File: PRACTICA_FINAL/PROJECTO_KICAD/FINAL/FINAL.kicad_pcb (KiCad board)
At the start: 4 copper layers, 100 x 56 mm, 111 parts, among them IC1 FT2232H, SW1 SWITCH-2CH-6P-3010010P1, SW2 EVQQ2, U1 ARDUINO_MEGA_SHIELD, U101 ATMEGA32U4-XUMU, U2 LTC3419MS, U3 93C56B, X1 12MHz, Y1 16Mhz KX-7

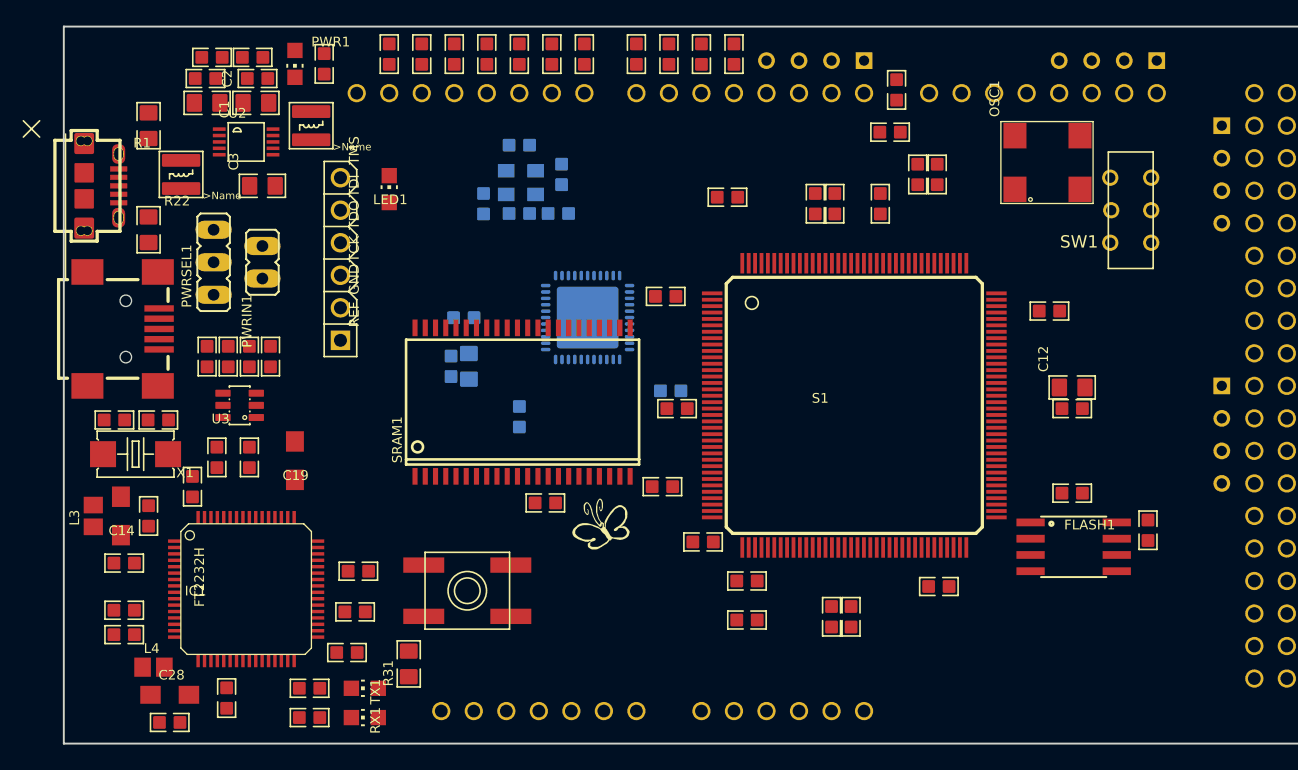
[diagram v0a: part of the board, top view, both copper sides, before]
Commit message: Agregados ultimos modelos 3D y tambien los agujeros de sujecion hasta aca estaria el trabajo.
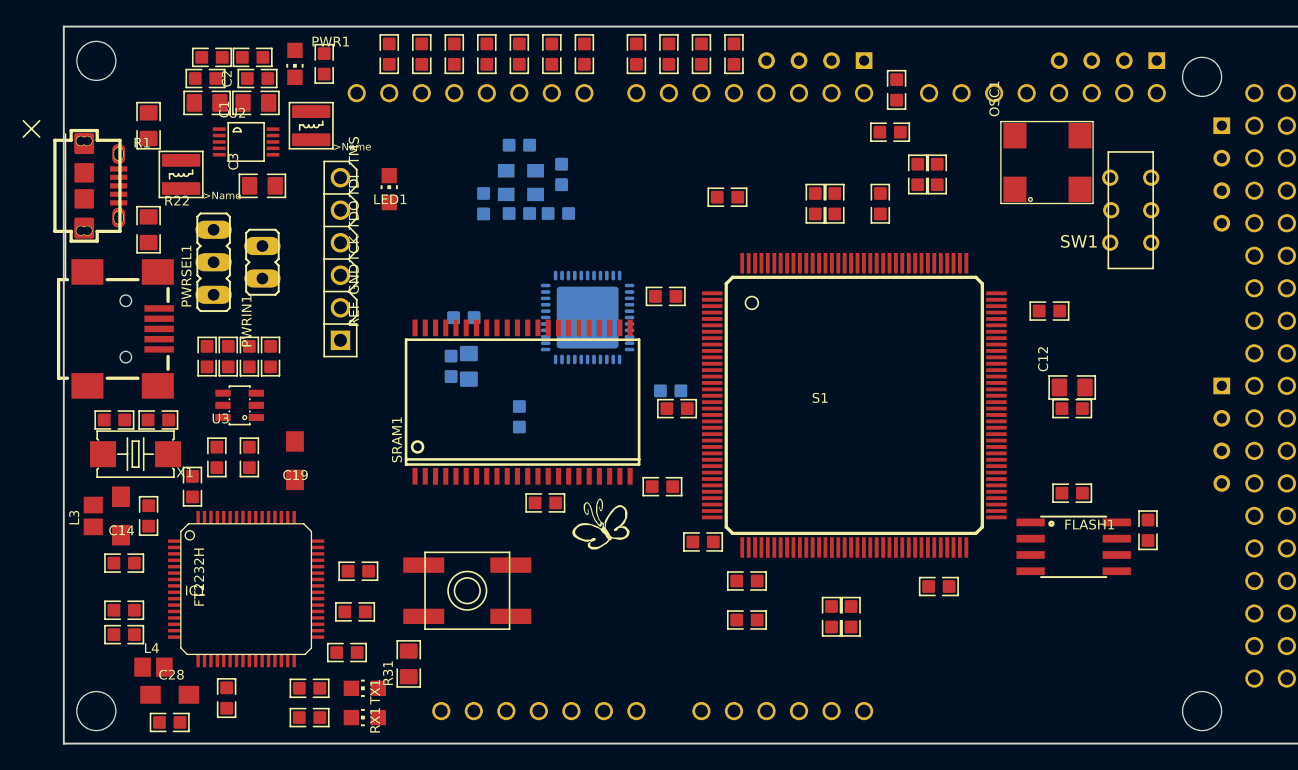
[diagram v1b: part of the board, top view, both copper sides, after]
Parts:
- added U$3: , Papilio_DUO:STAND-OFF-TIGHT, F.Cu at (187.4, 80.9)
- added U$3: , Papilio_DUO:STAND-OFF-TIGHT, F.Cu at (101.0, 130.5)
- added U$3: , Papilio_DUO:STAND-OFF-TIGHT, F.Cu at (101.0, 79.7)
- added U$3: , Papilio_DUO:STAND-OFF-TIGHT, F.Cu at (187.4, 130.5)
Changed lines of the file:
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@@
     (tracks 0)
     (zones 0)
-    (modules 111)
+    (modules 115)
     (nets 214)
   )
@@
   )
   (layers
-    (0 Top signal hide)
-    (1 Route2 signal hide)
-    (2 Route3 signal hide)
+    (0 Top signal)
+    (1 Route2 signal)
+    (2 Route3 signal)
     (31 Bottom signal)
     (32 B.Adhes user hide)
@@
     (34 B.Paste user hide)
     (35 F.Paste user hide)
-    (36 B.SilkS user hide)
+    (36 B.SilkS user)
     (37 F.SilkS user)
     (38 B.Mask user hide)
@@
     (mod_text_size 1 1)
     (mod_text_width 0.15)
-    (pad_size 1.524 1.524)
-    (pad_drill 0.762)
+    (pad_size 3.048 3.048)
+    (pad_drill 3.048)
     (pad_to_mask_clearance 0.2)
     (aux_axis_origin 0 0)
@@
     (add_net "Net-(WING_POWER6-PadP2)")
   )
+  (module Papilio_DUO:6P-2CH-2.54-9.1X3.5X3.2+2H (layer Top)
+    (at 181.8291 91.3476 90)
+    (fp_text reference SW1 (at -1.905 -2.54) (layer F.SilkS)
+      (effects (font (size 0.9652 0.9652) (thickness 0.14478)) (justify right top))
+    )
+    (fp_text value SWITCH-2CH-6P-3010010P1 (at -1.905 0.635 90) (layer F.Fab)
+      (effects (font (size 0.76 0.76) (thickness 0.1064)) (justify left bottom))
+    )
+    (fp_line (start -4.55 1.75) (end -4.55 -1.75) (layer F.SilkS) (width 0.127))
+    (fp_line (start -4.55 -1.75) (end 4.55 -1.75) (layer F.SilkS) (width 0.127))
+    (fp_line (start 4.55 -1.75) (end 4.55 1.75) (layer F.SilkS) (width 0.127))
+    (fp_line (start 4.55 1.75) (end -4.55 1.75) (layer F.SilkS) (width 0.127))
+    (fp_poly (pts (xy 4.55 1.75) (xy 4.55 -1.75) (xy -4.55 -1.75) (xy -4.55 1.75)) (layer Dwgs.User) (width 0))
+    (pad COM1 thru_hole circle (at 0 1.6 180) (size 1.27 1.27) (drill 0.8128) (layers *.Cu *.Mask)
+      (net 185 "Net-(SW1-PadCOM1)") (solder_mask_margin 0.0508))
+    (pad COM2 thru_hole circle (at 0 -1.524 180) (size 1.27 1.27) (drill 0.8128) (layers *.Cu *.Mask)
+      (net 177 /FPGA/FPGA-CORE/SW1) (solder_mask_margin 0.0508))
+    (pad CH1A thru_hole circle (at -2.54 1.6 180) (size 1.27 1.27) (drill 0.8128) (layers *.Cu *.Mask)
+      (net 186 "Net-(SW1-PadCH1A)") (solder_mask_margin 0.0508))
+    (pad CH1B thru_hole circle (at 2.54 1.6 180) (size 1.27 1.27) (drill 0.8128) (layers *.Cu *.Mask)
+      (net 187 "Net-(SW1-PadCH1B)") (solder_mask_margin 0.0508))
+    (pad CH2B thru_hole circle (at 2.54 -1.6 180) (size 1.27 1.27) (drill 0.8128) (layers *.Cu *.Mask)
+      (net 5 GND) (solder_mask_margin 0.0508))
+    (pad CH2A thru_hole circle (at -2.54 -1.6 180) (size 1.27 1.27) (drill 0.8128) (layers *.Cu *.Mask)
+      (net 6 +3V3) (solder_mask_margin 0.0508))
+    (model ${KISYS3DMOD}/Button_Switch_THT.3dshapes/SW_CuK_JS202011CQN_DPDT_Straight.step
+      (offset (xyz -2.5 1.75 0))
+      (scale (xyz 1 1 1))
+      (rotate (xyz 0 0 0))
+    )
+  )
+  (module Papilio_DUO:STAND-OFF-TIGHT (layer Top)
+    (at 187.4011 80.9336)
+    (descr "<b>Stand Off</b><p>\nThis is the mechanical footprint for a #4 phillips button head screw. Use the keepout ring to avoid running the screw head into surrounding components. SKU : PRT-00447")
+    (fp_text reference U$3 (at 0 0) (layer F.SilkS) hide
+      (effects (font (size 1.27 1.27) (thickness 0.15)))
+    )
+    (fp_text value "" (at 0 0) (layer F.SilkS) hide
+      (effects (font (size 1.27 1.27) (thickness 0.15)))
+    )
+    (fp_arc (start 0 0) (end 0 -1.8542) (angle 180) (layer Dwgs.User) (width 0.2032))
+    (fp_arc (start 0 0) (end 0 1.8542) (angle 180) (layer Dwgs.User) (width 0.2032))
+    (fp_arc (start 0 0) (end 0 1.8542) (angle -180) (layer Dwgs.User) (width 0.2032))
+    (fp_arc (start 0 0) (end 0 1.8542) (angle 180) (layer Dwgs.User) (width 0.2032))
+    (fp_circle (center 0 0) (end 2.794 0) (layer Dwgs.User) (width 0.127))
+    (pad "" np_thru_hole circle (at 0 0) (size 3.048 3.048) (drill 3.048) (layers *.Cu *.Mask))
+  )
+  (module Papilio_DUO:STAND-OFF-TIGHT (layer Top)
+    (at 101.0411 130.4636)
+    (descr "<b>Stand Off</b><p>\nThis is the mechanical footprint for a #4 phillips button head screw. Use the keepout ring to avoid running the screw head into surrounding components. SKU : PRT-00447")
+    (fp_text reference U$3 (at 3.94 -0.12) (layer F.SilkS) hide
+      (effects (font (size 1.27 1.27) (thickness 0.15)))
+    )
+    (fp_text value "" (at 0 0) (layer F.SilkS) hide
+      (effects (font (size 1.27 1.27) (thickness 0.15)))
+    )
+    (fp_arc (start 0 0) (end 0 -1.8542) (angle 180) (layer Dwgs.User) (width 0.2032))
+    (fp_arc (start 0 0) (end 0 1.8542) (angle 180) (layer Dwgs.User) (width 0.2032))
+    (fp_arc (start 0 0) (end 0 1.8542) (angle -180) (layer Dwgs.User) (width 0.2032))
+    (fp_arc (start 0 0) (end 0 1.8542) (angle 180) (layer Dwgs.User) (width 0.2032))
+    (fp_circle (center 0 0) (end 2.794 0) (layer Dwgs.User) (width 0.127))
+    (pad "" np_thru_hole circle (at 0 0) (size 3.048 3.048) (drill 3.048) (layers *.Cu *.Mask))
+  )
+  (module Papilio_DUO:STAND-OFF-TIGHT (layer Top)
+    (at 101.0411 79.6836)
+    (descr "<b>Stand Off</b><p>\nThis is the mechanical footprint for a #4 phillips button head screw. Use the keepout ring to avoid running the screw head into surrounding components. SKU : PRT-00447")
+    (fp_text reference U$3 (at 0 0) (layer F.SilkS) hide
+      (effects (font (size 1.27 1.27) (thickness 0.15)))
+    )
+    (fp_text value "" (at 0 0) (layer F.SilkS) hide
+      (effects (font (size 1.27 1.27) (thickness 0.15)))
+    )
+    (fp_arc (start 0 0) (end 0 -1.8542) (angle 180) (layer Dwgs.User) (width 0.2032))
+    (fp_arc (start 0 0) (end 0 1.8542) (angle 180) (layer Dwgs.User) (width 0.2032))
+    (fp_arc (start 0 0) (end 0 1.8542) (angle -180) (layer Dwgs.User) (width 0.2032))
+    (fp_arc (start 0 0) (end 0 1.8542) (angle 180) (layer Dwgs.User) (width 0.2032))
+    (fp_circle (center 0 0) (end 2.794 0) (layer Dwgs.User) (width 0.127))
+    (pad "" np_thru_hole circle (at 0 0) (size 3.048 3.048) (drill 3.048) (layers *.Cu *.Mask))
+  )
+  (module Papilio_DUO:STAND-OFF-TIGHT (layer Top)
+    (at 187.4011 130.4636)
+    (descr "<b>Stand Off</b><p>\nThis is the mechanical footprint for a #4 phillips button head screw. Use the keepout ring to avoid running the screw head into surrounding components. SKU : PRT-00447")
+    (fp_text reference U$3 (at 0 0) (layer F.SilkS) hide
+      (effects (font (size 1.27 1.27) (thickness 0.15)))
+    )
+    (fp_text value "" (at 0 0) (layer F.SilkS) hide
+      (effects (font (size 1.27 1.27) (thickness 0.15)))
+    )
+    (fp_arc (start 0 0) (end 0 -1.8542) (angle 180) (layer Dwgs.User) (width 0.2032))
+    (fp_arc (start 0 0) (end 0 1.8542) (angle 180) (layer Dwgs.User) (width 0.2032))
+    (fp_arc (start 0 0) (end 0 1.8542) (angle -180) (layer Dwgs.User) (width 0.2032))
+    (fp_arc (start 0 0) (end 0 1.8542) (angle 180) (layer Dwgs.User) (width 0.2032))
+    (fp_circle (center 0 0) (end 2.794 0) (layer Dwgs.User) (width 0.127))
+    (pad "" np_thru_hole circle (at 0 0) (size 3.048 3.048) (drill 3.048) (layers *.Cu *.Mask))
+  )
   (module Papilio_DUO:OSC1 (layer Top)
     (at 172.7867 89.722)
@@
     )
   )
-  (module Papilio_DUO:6P-2CH-2.54-9.1X3.5X3.2+2H (layer Top)
-    (at 181.8291 91.3476 90)
-    (fp_text reference SW1 (at -1.905 -2.54) (layer F.SilkS)
-      (effects (font (size 0.9652 0.9652) (thickness 0.14478)) (justify right top))
-    )
-    (fp_text value SWITCH-2CH-6P-3010010P1 (at -1.905 0.635 90) (layer F.Fab)
-      (effects (font (size 0.76 0.76) (thickness 0.1064)) (justify left bottom))
-    )
-    (fp_poly (pts (xy 4.55 1.75) (xy 4.55 -1.75) (xy -4.55 -1.75) (xy -4.55 1.75)) (layer Dwgs.User) (width 0))
-    (fp_line (start 4.55 1.75) (end -4.55 1.75) (layer F.SilkS) (width 0.127))
-    (fp_line (start 4.55 -1.75) (end 4.55 1.75) (layer F.SilkS) (width 0.127))
-    (fp_line (start -4.55 -1.75) (end 4.55 -1.75) (layer F.SilkS) (width 0.127))
-    (fp_line (start -4.55 1.75) (end -4.55 -1.75) (layer F.SilkS) (width 0.127))
-    (pad CH2A thru_hole circle (at -2.54 -1.6 180) (size 1.27 1.27) (drill 0.8128) (layers *.Cu *.Mask)
-      (net 6 +3V3) (solder_mask_margin 0.0508))
-    (pad CH2B thru_hole circle (at 2.54 -1.6 180) (size 1.27 1.27) (drill 0.8128) (layers *.Cu *.Mask)
-      (net 5 GND) (solder_mask_margin 0.0508))
-    (pad CH1B thru_hole circle (at 2.54 1.6 180) (size 1.27 1.27) (drill 0.8128) (layers *.Cu *.Mask)
-      (net 187 "Net-(SW1-PadCH1B)") (solder_mask_margin 0.0508))
-    (pad CH1A thru_hole circle (at -2.54 1.6 180) (size 1.27 1.27) (drill 0.8128) (layers *.Cu *.Mask)
-      (net 186 "Net-(SW1-PadCH1A)") (solder_mask_margin 0.0508))
-    (pad COM2 thru_hole circle (at 0 -1.524 180) (size 1.27 1.27) (drill 0.8128) (layers *.Cu *.Mask)
-      (net 177 /FPGA/FPGA-CORE/SW1) (solder_mask_margin 0.0508))
-    (pad COM1 thru_hole circle (at 0 1.6 180) (size 1.27 1.27) (drill 0.8128) (layers *.Cu *.Mask)
-      (net 185 "Net-(SW1-PadCOM1)") (solder_mask_margin 0.0508))
-  )
   (module Papilio_DUO:CHIP-LED0805 (layer Top)

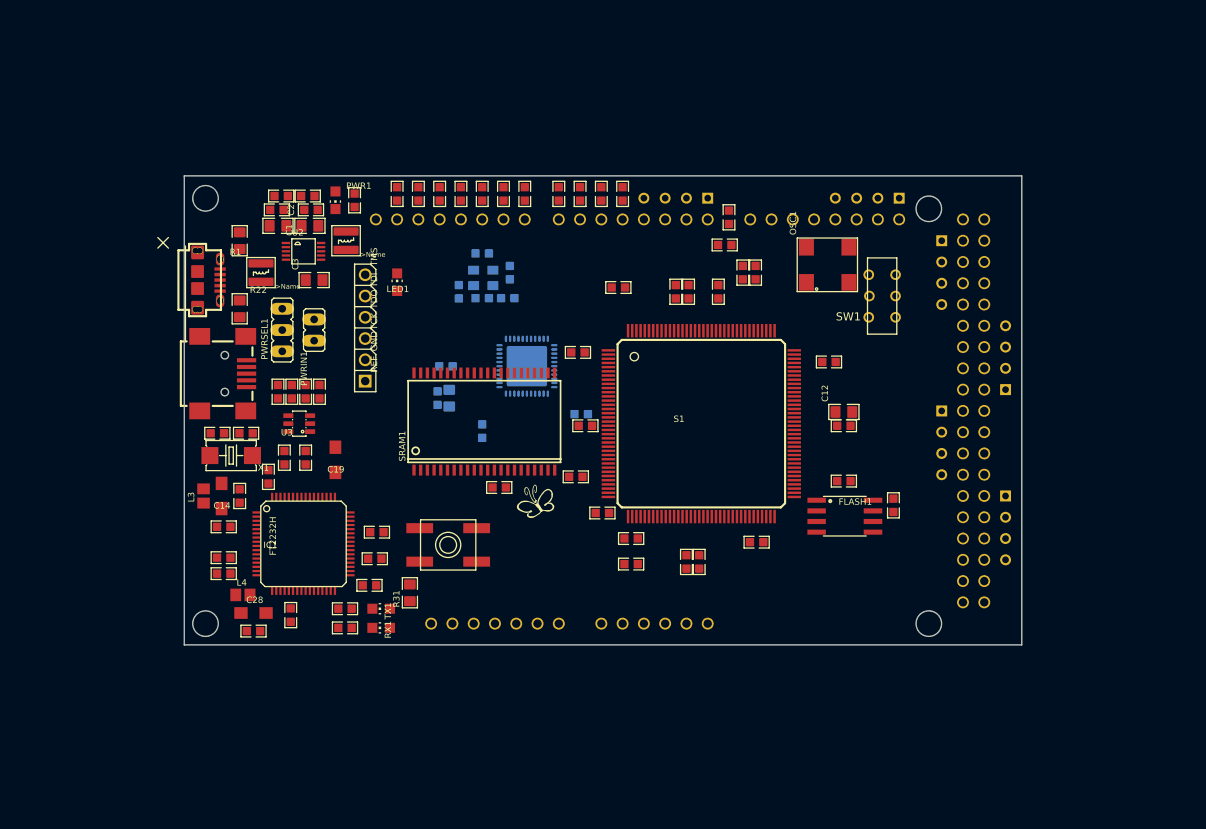
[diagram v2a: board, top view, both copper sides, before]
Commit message: Se agregan las imagenes de las vistas en 3D. Tambien se configurar los coopper pour y ademas se tiran algunas pistas y algunas vias termicas.
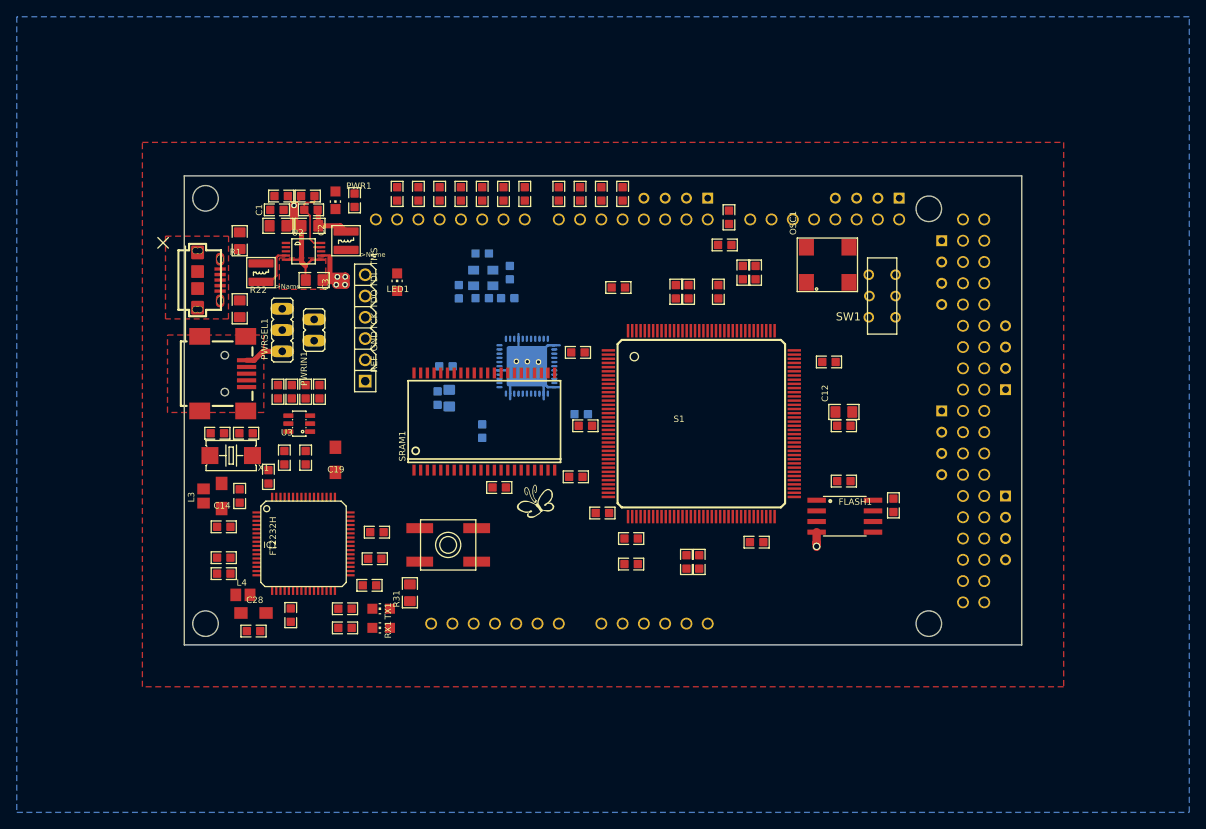
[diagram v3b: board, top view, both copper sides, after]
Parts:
- turned C1 to 0 degrees
- turned C2 to 180 degrees
- turned C3 to 180 degrees
- turned R3 to 0 degrees
- turned R4 to 180 degrees
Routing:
- net GND: track 0.00 -> 47.2 mm, vias 0 -> 5
- net +5V: track 0.00 -> 8.70 mm, vias 0 -> 4
- net Net-(R4-Pad1): track 0.00 -> 8.01 mm
- net Net-(L1-Pad1): track 0.00 -> 5.59 mm
- net +1V2: track 0.00 -> 5.53 mm
- net /FT2232H/5V_FT2232: track 0.00 -> 4.70 mm
- net +3V3: track 0.00 -> 0.84 mm
- added copper zone on F.Cu, net +3V3
- added copper zone on Route3, net +3V3
- added copper zone on B.Cu, net GND
- added copper zone on F.Cu, net GND
- added copper zone on Route2, net GND
